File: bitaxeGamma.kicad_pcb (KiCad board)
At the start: 4 copper layers, 56.5 x 99.8 mm, 146 parts, among them J1 54-00164, J2 TC2030-IDC, J3 Conn_01x04, J4 Conn_01x06, J5 USB_C_Receptacle_USB2.0, J6 Conn_01x04, J7 Conn_01x04, SW1 GT-TC029B-H025-L1N, SW2 GT-TC029B-H025-L1N, T1 net-tie, U10 EMC2101, U2 TPS546D24ARVFR, U3 RT9080-33GJ5, U4 ESP32-S3-WROOM-1, U5 MCP1824T-1202E/OT, U6 MCP1824T-0802E, U7 25MHz, U8 BM1370_mode1, U9 SN74AVC4T774

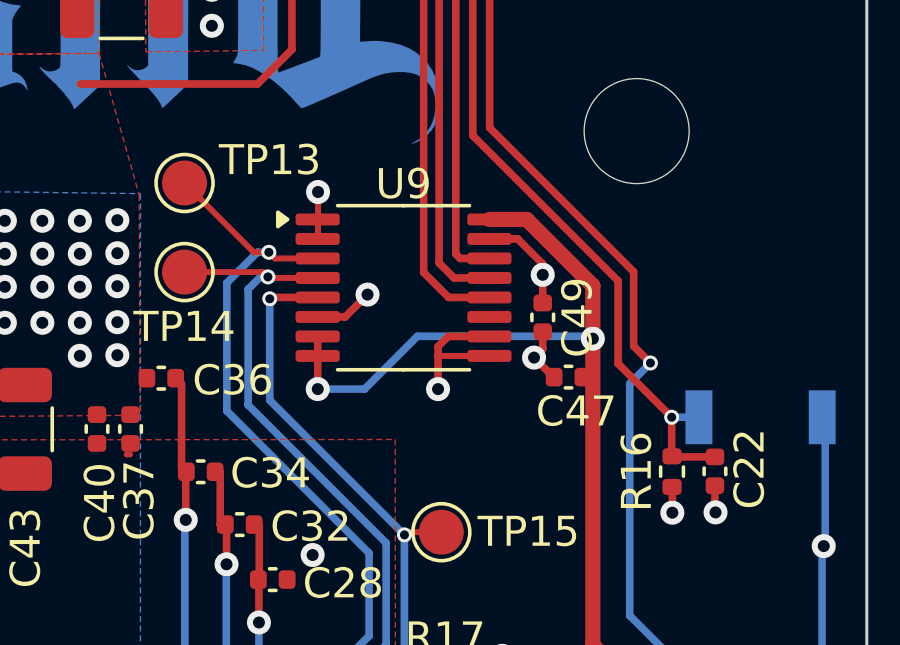
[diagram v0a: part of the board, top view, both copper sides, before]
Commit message: Revert "bump version to 602. remove R21 and fix for #6"
This reverts commit 8bd74c865f9910776743c8aa45b35babe35214af.
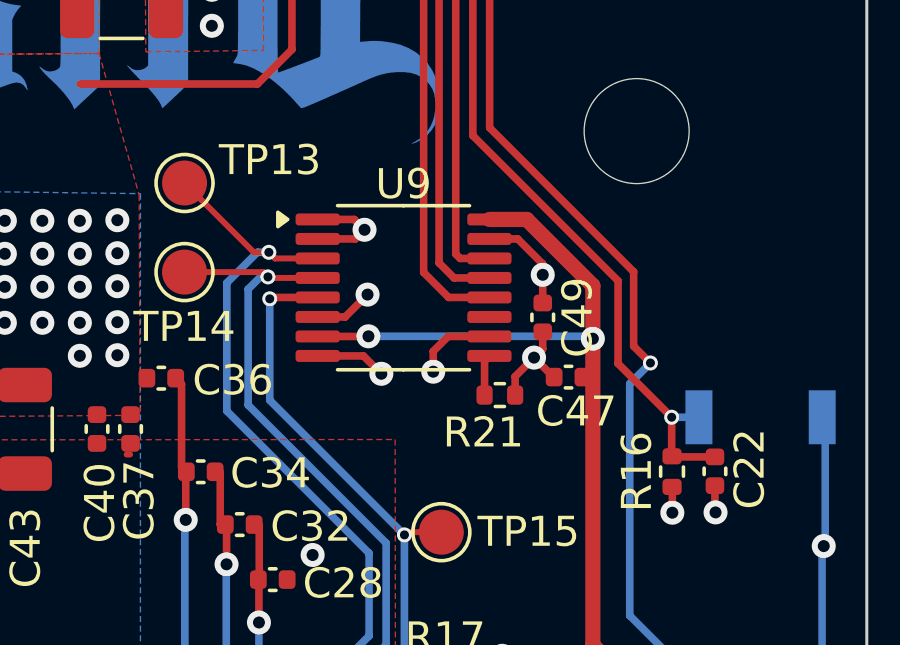
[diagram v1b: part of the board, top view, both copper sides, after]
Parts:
- added R21: 20k, Resistor_SMD:R_0402_1005Metric, F.Cu at (121.5, 103.7)
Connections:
- U9 pad 8: /BM1370/1V2 -> GND
- U9 pad 9: GND -> Net-(U9-OE)
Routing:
- net GND: track 97.0 -> 100.5 mm, vias 81 -> 82
- net /BM1370/1V2: track 77.1 -> 74.6 mm
- net Net-(U9-OE): track 0.00 -> 1.37 mm
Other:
- board text added: "601"
- board text removed: "602"
